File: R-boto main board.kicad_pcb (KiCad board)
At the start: 2 copper layers, 91.4 x 71.1 mm, 4 parts

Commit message: outline complete
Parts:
- added REF**: OSHW-Logo2_7.3x6mm_SilkScreen, Symbol:OSHW-Logo2_7.3x6mm_SilkScreen, F.Cu at (178.4, 118.7)
- F1 - 3.5mm: renamed from REF**
- F2 - 3.5mm: renamed from REF**
- F3 - 3.5mm: renamed from REF**
- F4 - 3.5mm: renamed from REF**
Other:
- board text added: "Microcontroller"
- board text added: "Power"
- board text added: "Wireless"

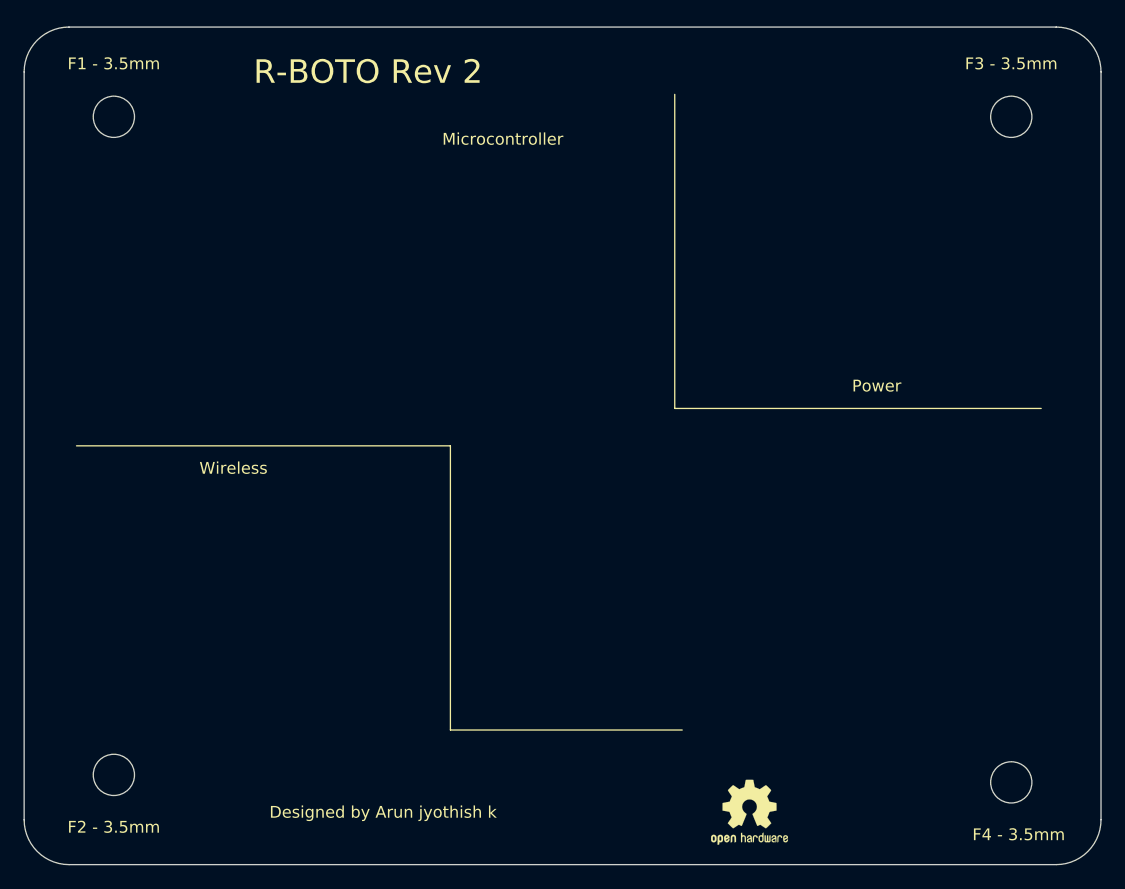
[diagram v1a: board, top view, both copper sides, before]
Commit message: schematic connector add
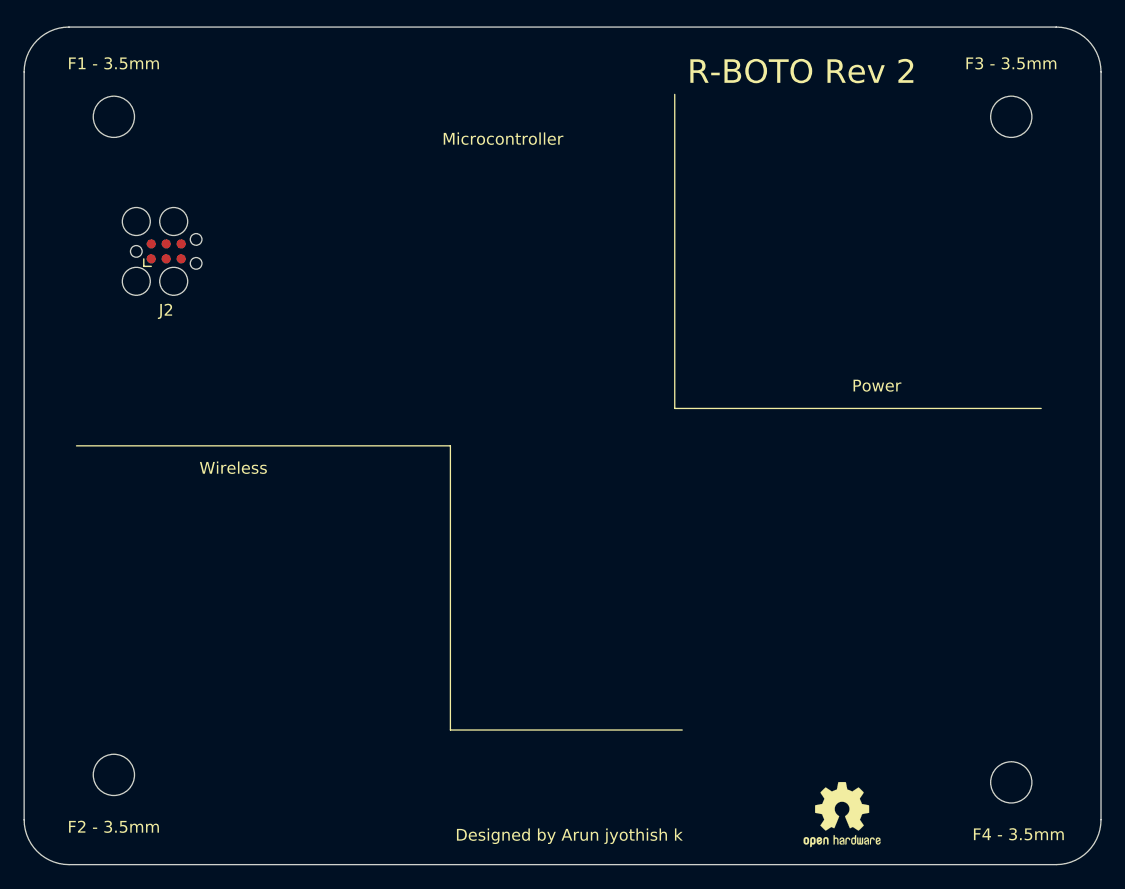
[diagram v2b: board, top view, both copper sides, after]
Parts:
- added J2: Conn_ARM_SWD_TagConnect_TC2030, Connector:Tag-Connect_TC2030-IDC-FP_2x03_P1.27mm_Vertical, F.Cu at (128.9, 71.1)
- moved REF** 7.86 mm to (186.3, 118.9)
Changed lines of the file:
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@@
   )
   (net 0 "")
+  (net 1 "unconnected-(J2-Pad1)")
+  (net 2 "unconnected-(J2-Pad2)")
+  (net 3 "unconnected-(J2-Pad3)")
+  (net 4 "unconnected-(J2-Pad4)")
+  (net 5 "unconnected-(J2-Pad5)")
+  (net 6 "unconnected-(J2-Pad6)")
   (footprint "Symbol:OSHW-Logo2_7.3x6mm_SilkScreen" (layer "F.Cu")
-    (at 178.435 118.745)
+    (at 186.295263 118.938383)
     (descr "Open Source Hardware Symbol")
     (tags "Logo Symbol OSHW")
@@
     (pad "" np_thru_hole circle (at 0 0) (size 3.5 3.5) (drill 3.5) (layers *.Cu *.Mask))
   )
+  (footprint "Connector:Tag-Connect_TC2030-IDC-FP_2x03_P1.27mm_Vertical" (layer "F.Cu")
+    (at 128.905 71.12)
+    (descr "Tag-Connect programming header; http://www.tag-connect.com/Materials/TC2030-IDC.pdf")
+    (tags "tag connect programming header pogo pins")
+    (property "Sheetfile" "R-boto main board.kicad_sch")
+    (property "Sheetname" "")
+    (property "exclude_from_bom" "")
+    (attr exclude_from_pos_files exclude_from_bom)
+    (fp_text reference "J2" (at 0 5) (layer "F.SilkS")
+      (effects (font (size 1 1) (thickness 0.15)))
+    )
+    (fp_text value "Conn_ARM_SWD_TagConnect_TC2030" (at 0 -4.7) (layer "F.Fab")
+      (effects (font (size 1 1) (thickness 0.15)))
+    )
+    (fp_text user "KEEPOUT" (at 0 0) (layer "Cmts.User")
+      (effects (font (size 0.4 0.4) (thickness 0.07)))
+    )
+    (fp_text user "${REFERENCE}" (at 0 0) (layer "F.Fab")
+      (effects (font (size 1 1) (thickness 0.15)))
+    )
+    (fp_line (start -1.905 1.27) (end -1.905 0.635) (layer "F.SilkS") (width 0.12))
+    (fp_line (start -1.27 1.27) (end -1.905 1.27) (layer "F.SilkS") (width 0.12))
+    (fp_line (start -4.25 4.25) (end -4.25 -4.25) (layer "F.CrtYd") (width 0.05))
+    (fp_line (start -4.25 -4.25) (end 3.75 -4.25) (layer "F.CrtYd") (width 0.05))
+    (fp_line (start 3.75 -4.25) (end 3.75 4.25) (layer "F.CrtYd") (width 0.05))
+    (fp_line (start 3.75 4.25) (end -4.25 4.25) (layer "F.CrtYd") (width 0.05))
+    (pad "" np_thru_hole circle (at 0.635 2.54) (size 2.3749 2.3749) (drill 2.3749) (layers *.Cu *.Mask))
+    (pad "" np_thru_hole circle (at -2.54 2.54) (size 2.3749 2.3749) (drill 2.3749) (layers *.Cu *.Mask))
+    (pad "" np_thru_hole circle (at 2.54 1.016) (size 0.9906 0.9906) (drill 0.9906) (layers *.Cu *.Mask))
+    (pad "" np_thru_hole circle (at -2.54 0) (size 0.9906 0.9906) (drill 0.9906) (layers *.Cu *.Mask))
+    (pad "" np_thru_hole circle (at 0.635 -2.54) (size 2.3749 2.3749) (drill 2.3749) (layers *.Cu *.Mask))
+    (pad "" np_thru_hole circle (at -2.54 -2.54) (size 2.3749 2.3749) (drill 2.3749) (layers *.Cu *.Mask))
+    (pad "" np_thru_hole circle (at 2.54 -1.016) (size 0.9906 0.9906) (drill 0.9906) (layers *.Cu *.Mask))
+    (pad "1" connect circle (at -1.27 0.635) (size 0.7874 0.7874) (layers "F.Cu" "F.Mask")
+      (net 1 "unconnected-(J2-Pad1)") (pinfunction "VCC") (pintype "power_in"))
+    (pad "2" connect circle (at -1.27 -0.635) (size 0.7874 0.7874) (layers "F.Cu" "F.Mask")
+      (net 2 "unconnected-(J2-Pad2)") (pinfunction "SWDIO") (pintype "bidirectional"))
+    (pad "3" connect circle (at 0 0.635) (size 0.7874 0.7874) (layers "F.Cu" "F.Mask")
+      (net 3 "unconnected-(J2-Pad3)") (pinfunction "~{RESET}") (pintype "open_collector"))
+    (pad "4" connect circle (at 0 -0.635) (size 0.7874 0.7874) (layers "F.Cu" "F.Mask")
+      (net 4 "unconnected-(J2-Pad4)") (pinfunction "SWCLK") (pintype "output"))
+    (pad "5" connect circle (at 1.27 0.635) (size 0.7874 0.7874) (layers "F.Cu" "F.Mask")
+      (net 5 "unconnected-(J2-Pad5)") (pinfunction "GND") (pintype "power_in"))
+    (pad "6" connect circle (at 1.27 -0.635) (size 0.7874 0.7874) (layers "F.Cu" "F.Mask")
+      (net 6 "unconnected-(J2-Pad6)") (pinfunction "SWO") (pintype "input"))
+    (zone (net 0) (net_name "") (layer "F.Cu") (hatch full 0.508)
+      (connect_pads (clearance 0))
+      (min_thickness 0.254)
+      (keepout (tracks allowed) (vias not_allowed) (pads allowed) (copperpour not_allowed) (footprints not_allowed))
+      (fill (thermal_gap 0.508) (thermal_bridge_width 0.508))
+      (polygon
+        (pts
+          (xy 130.175 70.485)
+          (xy 127.635 70.485)
+          (xy 127.635 71.755)
+          (xy 130.175 71.755)
+        )
+      )
+    )
+  )
   (gr_line (start 172.085 84.455) (end 203.2 84.455) (layer "F.SilkS") (width 0.1))
   (gr_line (start 172.085 57.785) (end 172.085 84.455) (layer "F.SilkS") (width 0.1))
@@
     (effects (font (size 1 1) (thickness 0.25)))
   )
-  (gr_text "R-BOTO Rev 2" (at 146.05 55.88) (layer "F.SilkS")
+  (gr_text "R-BOTO Rev 2" (at 182.88 55.88) (layer "F.SilkS")
     (effects (font (size 2 2) (thickness 0.5)))
   )
-  (gr_text "Designed by Arun jyothish k" (at 147.32 118.745) (layer "F.SilkS")
+  (gr_text "Designed by Arun jyothish k" (at 163.11413 120.69313) (layer "F.SilkS")
     (effects (font (size 1 1) (thickness 0.25)))
   )

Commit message: component placing
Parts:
- added BZ1: Buzzer, Buzzer_Beeper:MagneticBuzzer_Kingstate_KCG0601, F.Cu at (189.8, 110.5)
- added D1: BOOT, Connector_PinHeader_2.54mm:PinHeader_1x04_P2.54mm_Vertical, F.Cu at (198.1, 88.3)
- added D2: ERROR, LED_SMD:LED_0805_2012Metric_Pad1.15x1.40mm_HandSolder, F.Cu at (127.0, 84.9)
- added D3: RUN, LED_SMD:LED_0805_2012Metric_Pad1.15x1.40mm_HandSolder, F.Cu at (133.3, 84.9)
- added D4: BAT LOW, LED_SMD:LED_0805_2012Metric_Pad1.15x1.40mm_HandSolder, F.Cu at (198.3, 80.3)
- added D5: CHARGING, LED_SMD:LED_0805_2012Metric_Pad1.15x1.40mm_HandSolder, F.Cu at (177.8, 81.3)
- added D6: BAT FULL, LED_SMD:LED_0805_2012Metric_Pad1.15x1.40mm_HandSolder, F.Cu at (198.4, 76.4)
- added D7: DATA, LED_SMD:LED_0805_2012Metric_Pad1.15x1.40mm_HandSolder, F.Cu at (157.5, 109.2)
- added J1: GPIO, Connector_PinHeader_2.54mm:PinHeader_2x20_P2.54mm_Vertical, F.Cu at (133.3, 57.8)
- added J10: BRL, jyothu footprint:3 pin connector solder pad, B.Cu at (158.0, 105.0)
- added J11: FLL, jyothu footprint:3 pin connector solder pad, B.Cu at (182.3, 96.7)
- added J12: BLL, jyothu footprint:3 pin connector solder pad, B.Cu at (141.6, 108.6)
- added J13: BLM, jyothu footprint:3 pin connector solder pad, B.Cu at (158.0, 96.5)
- added J14: FRM, jyothu footprint:3 pin connector solder pad, B.Cu at (141.6, 103.7)
- added J15: BRM, jyothu footprint:3 pin connector solder pad, B.Cu at (182.3, 92.7)
- added J16: FLM, jyothu footprint:3 pin connector solder pad, B.Cu at (182.3, 101.6)
- added J17: FLT, jyothu footprint:3 pin connector solder pad, B.Cu at (158.0, 92.3)
- added J18: BLT, jyothu footprint:3 pin connector solder pad, B.Cu at (141.6, 94.6)
- added J19: FRT, jyothu footprint:3 pin connector solder pad, B.Cu at (158.0, 100.5)
- added J20: BRT, jyothu footprint:3 pin connector solder pad, B.Cu at (182.3, 106.0)
- added J21: OLED, jyothu footprint:4pin connector solder pad, F.Cu at (138.7, 80.9)
- added J3: 3.3V IN, Connector_PinHeader_2.54mm:PinHeader_1x02_P2.54mm_Vertical, F.Cu at (205.7, 78.7)
- added J4: 5V IN, Connector_PinHeader_2.54mm:PinHeader_1x02_P2.54mm_Vertical, F.Cu at (190.1, 55.1)
- added J5: ULTR 1, jyothu footprint:4pin connector solder pad, B.Cu at (118.1, 68.6)
- added J6: ULTR 3, jyothu footprint:4pin connector solder pad, B.Cu at (117.9, 105.4)
- added J7: ULTR 2, jyothu footprint:4pin connector solder pad, B.Cu at (207.2, 69.8)
- added J8: ULTR 4, jyothu footprint:4pin connector solder pad, B.Cu at (207.2, 108.6)
- added J9: FRL, jyothu footprint:3 pin connector solder pad, B.Cu at (141.6, 98.4)
- added R1: Ambient Light Sensor, OptoDevice:R_LDR_5.1x4.3mm_P3.4mm_Vertical, F.Cu at (165.8, 64.4)
- J2: value Conn_ARM_SWD_TagConnect_TC2030 -> SWD
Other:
- board text added: "SWD"
